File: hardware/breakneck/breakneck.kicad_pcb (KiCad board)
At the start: 2 copper layers, 53.3 x 64 mm, 112 parts, among them J1 CONN_WEST, J10 GS2, J12 CONN_JTAG_6P, J15 GS2, J16 CONN_JST, J2 CONN_DEDI, J3 CONN_OLED, J4 USB_C_Rcpt_Min, J5 CONN_SOUTH, J6 CONN_EAST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

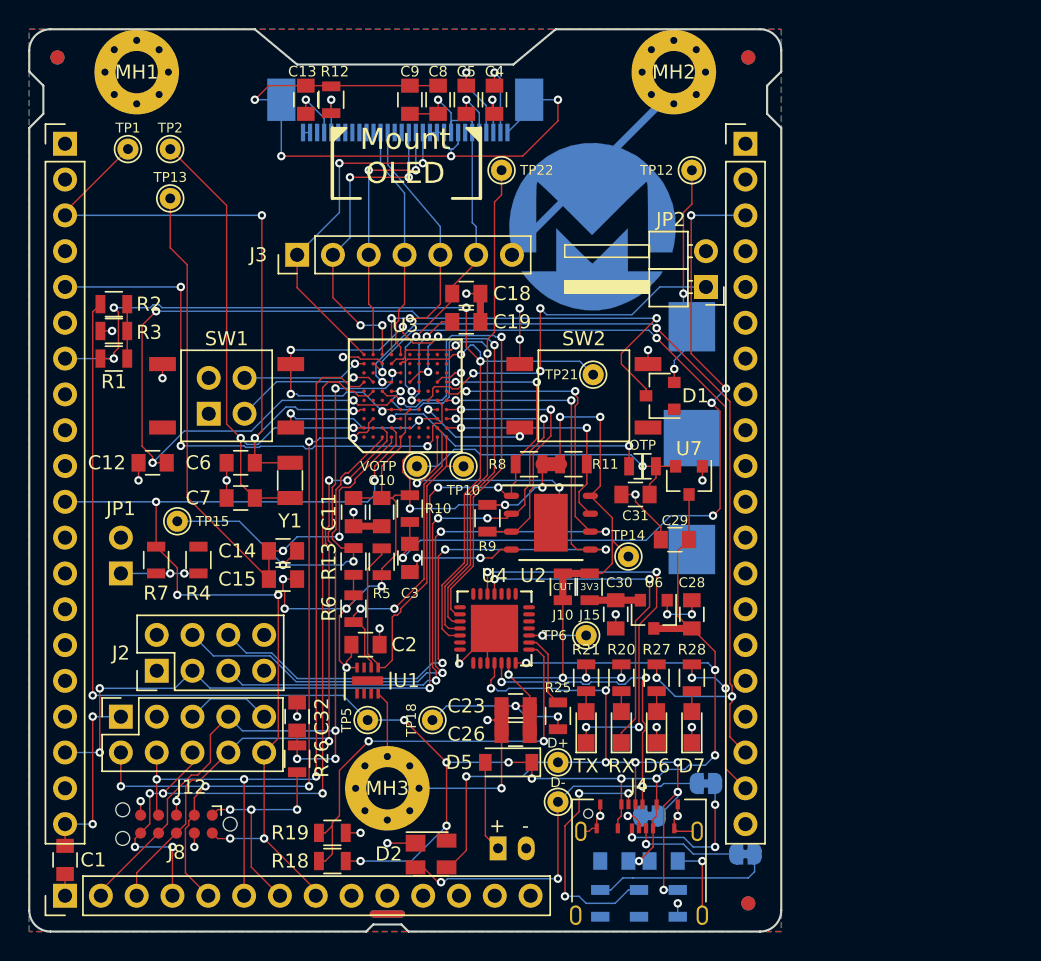
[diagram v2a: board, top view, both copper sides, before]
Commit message: Added slide switch (hack) and supporting circuitry to decouple lipo.
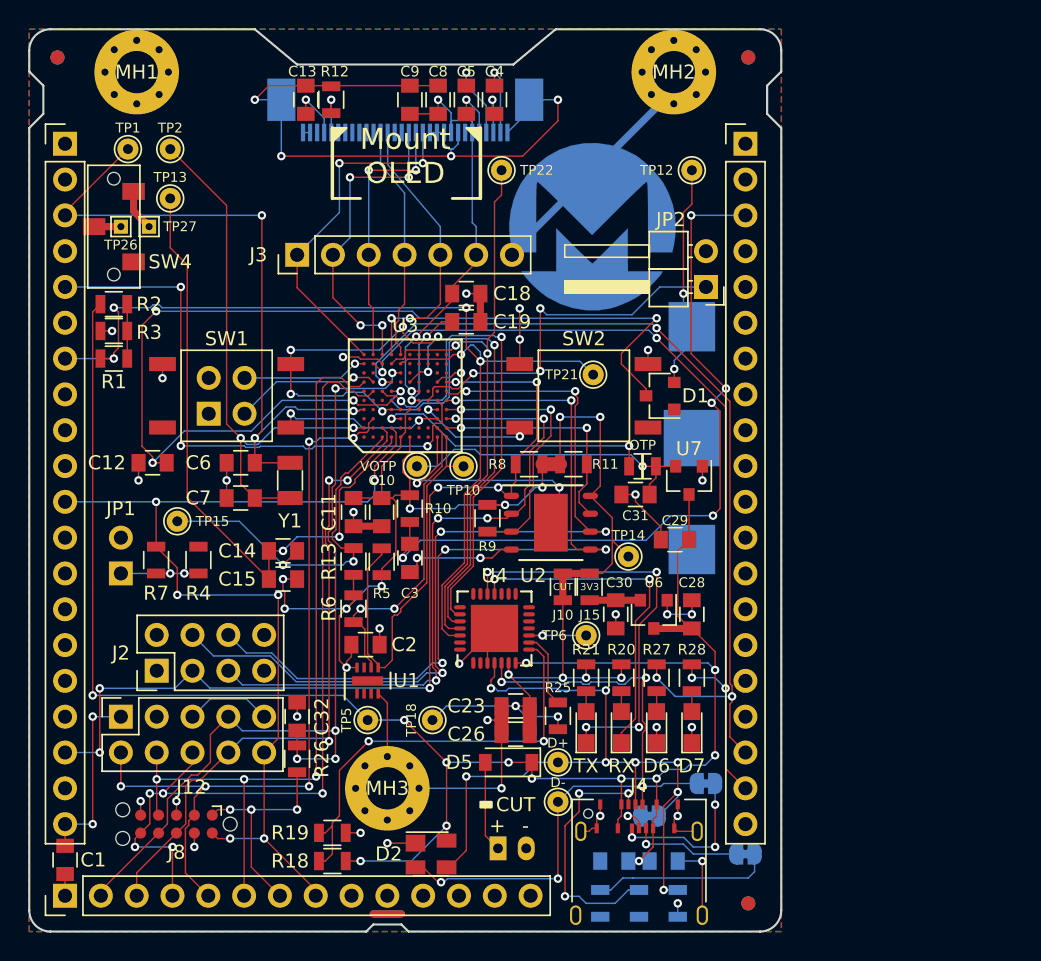
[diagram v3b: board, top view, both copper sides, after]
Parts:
- added SW4: SW_SPDT, Monero_Local:SW_SPDT_CLSB-12A, F.Cu at (106.0, 78.0)
- added TP26: TEST, Monero_Local:TestPoint_THTPad_1.0x1.0mm_Drill0.5mm, F.Cu at (106.5, 78.0)
- added TP27: TEST, Monero_Local:TestPoint_THTPad_1.0x1.0mm_Drill0.5mm, F.Cu at (108.5, 78.0)
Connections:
- J16 pad 1: Net-(D5-Pad2) -> Net-(J16-Pad1)
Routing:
- net Net-(J16-Pad1): track 0.00 -> 2.96 mm
- net Net-(D5-Pad2): track 6.47 -> 8.37 mm
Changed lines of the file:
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@@
   (general
     (thickness 1.6)
-    (drawings 146)
-    (tracks 1271)
+    (drawings 148)
+    (tracks 1274)
     (zones 0)
-    (modules 112)
-    (nets 161)
+    (modules 115)
+    (nets 163)
   )
   (page A4)
@@
   (net 159 "Net-(J4-PadB6)")
   (net 160 "Net-(JP5-Pad2)")
+  (net 161 "Net-(J16-Pad1)")
+  (net 162 "Net-(SW4-Pad1)")
   (net_class Default "This is the default net class."
     (clearance 0.1016)
@@
     (add_net "Net-(J1-Pad17)")
     (add_net "Net-(J1-Pad9)")
+    (add_net "Net-(J16-Pad1)")
     (add_net "Net-(J2-Pad7)")
     (add_net "Net-(J2-Pad8)")
@@
     (add_net "Net-(SW2-Pad2)")
     (add_net "Net-(SW3-Pad2)")
+    (add_net "Net-(SW4-Pad1)")
     (add_net "Net-(TP6-Pad1)")
     (add_net "Net-(U1-Pad1)")
@@
       (net 1 GND))
     (pad 1 thru_hole rect (at 0 0) (size 1.2 1.7) (drill 0.7) (layers *.Cu *.Mask)
-      (net 53 "Net-(D5-Pad2)"))
+      (net 161 "Net-(J16-Pad1)"))
     (model ${KIPRJMOD}/modules/packages3d/Connectors_JST.3dshapes/JST_PH_B2B-PH-K_02x2.00mm_Straight.wrl
       (at (xyz 0 0 0))
@@
       ))
   )
+  (module Monero_Local:SW_SPDT_CLSB-12A (layer F.Cu)
+    (at 106 78 90)
+    (descr https://www.nidec-copal-electronics.com/e/catalog/switch/cl-sb.pdf)
+    (tags "switch spdt")
+    (attr smd)
+    (fp_text reference SW4 (at -2.5 4 180) (layer F.SilkS)
+      (effects (font (size 1 1) (thickness 0.15)))
+    )
+    (fp_text value SW_SPDT (at 0 3.81 90) (layer F.Fab)
+      (effects (font (size 1 1) (thickness 0.15)))
+    )
+    (fp_line (start -4.25 -1.75) (end 4.25 -1.75) (layer F.Fab) (width 0.1))
+    (fp_line (start 4.25 -1.75) (end 4.25 1.75) (layer F.Fab) (width 0.1))
+    (fp_line (start 4.25 1.75) (end -4.25 1.75) (layer F.Fab) (width 0.1))
+    (fp_line (start -4.25 -1.75) (end -4.25 1.75) (layer F.Fab) (width 0.1))
+    (fp_text user %R (at 0 0 90) (layer F.Fab)
+      (effects (font (size 1 1) (thickness 0.15)))
+    )
+    (fp_line (start -4.35 -1.85) (end 4.35 -1.85) (layer F.SilkS) (width 0.12))
+    (fp_line (start 4.35 -1.85) (end 4.35 1.85) (layer F.SilkS) (width 0.12))
+    (fp_line (start -4.35 1.85) (end -4.35 -1.85) (layer F.SilkS) (width 0.12))
+    (fp_line (start -4.35 1.85) (end 4.35 1.85) (layer F.SilkS) (width 0.12))
+    (fp_line (start -4.75 -2.25) (end -4.75 2.25) (layer F.CrtYd) (width 0.05))
+    (fp_line (start -4.75 2.25) (end 4.75 2.25) (layer F.CrtYd) (width 0.05))
+    (fp_line (start 4.75 2.25) (end 4.75 -2.25) (layer F.CrtYd) (width 0.05))
+    (fp_line (start -4.75 -2.25) (end 4.75 -2.25) (layer F.CrtYd) (width 0.05))
+    (pad 1 smd rect (at -2.5 1.4 90) (size 1.2 1.6) (layers F.Cu F.Paste F.Mask)
+      (net 162 "Net-(SW4-Pad1)"))
+    (pad 2 smd rect (at 0 -1.4 90) (size 1.2 1.6) (layers F.Cu F.Paste F.Mask)
+      (net 53 "Net-(D5-Pad2)"))
+    (pad 3 smd rect (at 2.5 1.4 90) (size 1.2 1.6) (layers F.Cu F.Paste F.Mask)
+      (net 161 "Net-(J16-Pad1)"))
+    (pad "" np_thru_hole circle (at -3.4 0 90) (size 0.9 0.9) (drill 0.9) (layers *.Cu *.Mask))
+    (pad "" np_thru_hole circle (at 3.4 0 90) (size 0.9 0.9) (drill 0.9) (layers *.Cu *.Mask))
+    (model ${KIPRJMOD}/modules/packages3d/Buttons_Switches_SMD.3dshapes/SW_SPDT_CLSB-12A.wrl
+      (offset (xyz 0 0 3.5))
+      (scale (xyz 0.4 0.4 0.4))
+      (rotate (xyz -90 0 0))
+    )
+  )
+  (module Monero_Local:TestPoint_THTPad_1.0x1.0mm_Drill0.5mm (layer F.Cu)
+    (at 106.5 78)
+    (descr "THT rectangular pad as test Point, square 1.0mm side length, hole diameter 0.5mm")
+    (tags "test point THT pad rectangle square")
+    (attr virtual)
+    (fp_text reference TP26 (at 0 1.3) (layer F.SilkS)
+      (effects (font (size 0.7 0.7) (thickness 0.1)))
+    )
+    (fp_text value TEST (at 0 1.55) (layer F.Fab)
+      (effects (font (size 1 1) (thickness 0.15)))
+    )
+    (fp_line (start 1 1) (end -1 1) (layer F.CrtYd) (width 0.05))
+    (fp_line (start 1 1) (end 1 -1) (layer F.CrtYd) (width 0.05))
+    (fp_line (start -1 -1) (end -1 1) (layer F.CrtYd) (width 0.05))
+    (fp_line (start -1 -1) (end 1 -1) (layer F.CrtYd) (width 0.05))
+    (fp_line (start -0.7 0.7) (end -0.7 -0.7) (layer F.SilkS) (width 0.12))
+    (fp_line (start 0.7 0.7) (end -0.7 0.7) (layer F.SilkS) (width 0.12))
+    (fp_line (start 0.7 -0.7) (end 0.7 0.7) (layer F.SilkS) (width 0.12))
+    (fp_line (start -0.7 -0.7) (end 0.7 -0.7) (layer F.SilkS) (width 0.12))
+    (fp_text user %R (at 0 -1.45) (layer F.Fab)
+      (effects (font (size 1 1) (thickness 0.15)))
+    )
+    (pad 1 thru_hole rect (at 0 0) (size 1 1) (drill 0.5) (layers *.Cu *.Mask)
+      (net 53 "Net-(D5-Pad2)"))
+  )
+  (module Monero_Local:TestPoint_THTPad_1.0x1.0mm_Drill0.5mm (layer F.Cu)
+    (at 108.5 78)
+    (descr "THT rectangular pad as test Point, square 1.0mm side length, hole diameter 0.5mm")
+    (tags "test point THT pad rectangle square")
+    (attr virtual)
+    (fp_text reference TP27 (at 2.2 0) (layer F.SilkS)
+      (effects (font (size 0.7 0.7) (thickness 0.1)))
+    )
+    (fp_text value TEST (at 0 1.55) (layer F.Fab)
+      (effects (font (size 1 1) (thickness 0.15)))
+    )
+    (fp_text user %R (at 0 -1.45) (layer F.Fab)
+      (effects (font (size 1 1) (thickness 0.15)))
+    )
+    (fp_line (start -0.7 -0.7) (end 0.7 -0.7) (layer F.SilkS) (width 0.12))
+    (fp_line (start 0.7 -0.7) (end 0.7 0.7) (layer F.SilkS) (width 0.12))
+    (fp_line (start 0.7 0.7) (end -0.7 0.7) (layer F.SilkS) (width 0.12))
+    (fp_line (start -0.7 0.7) (end -0.7 -0.7) (layer F.SilkS) (width 0.12))
+    (fp_line (start -1 -1) (end 1 -1) (layer F.CrtYd) (width 0.05))
+    (fp_line (start -1 -1) (end -1 1) (layer F.CrtYd) (width 0.05))
+    (fp_line (start 1 1) (end 1 -1) (layer F.CrtYd) (width 0.05))
+    (fp_line (start 1 1) (end -1 1) (layer F.CrtYd) (width 0.05))
+    (pad 1 thru_hole rect (at 0 0) (size 1 1) (drill 0.5) (layers *.Cu *.Mask)
+      (net 161 "Net-(J16-Pad1)"))
+  )
+  (gr_poly (pts (xy 132 119.2) (xy 132.8 119.2) (xy 132.8 118.8) (xy 132 118.8)) (layer F.SilkS) (width 0.15))
+  (gr_text CUT (at 134.5 119) (layer F.SilkS)
+    (effects (font (size 1 1) (thickness 0.2)))
+  )
   (dimension 64 (width 0.3) (layer Dwgs.User)
     (gr_text "64,000 mm" (at 94.15 96 270) (layer Dwgs.User)
@@
   (segment (start 143.702401 113.697599) (end 143.5 113.9) (width 0.1016) (layer F.Cu) (net 31))
   (segment (start 142.25 110.46) (end 142.71 110) (width 0.1016) (layer B.Cu) (net 31))
-  (segment (start 142.75 121.325) (end 142.75 120.68) (width 0.1016) (layer F.Cu) (net 158) (status 30))
   (segment (start 143.5 117.7) (end 143.5 118.98) (width 0.1016) (layer F.Cu) (net 31) (status 20))
   (via (at 143.5 117.7) (size 0.6) (drill 0.3) (layers F.Cu B.Cu) (net 31))
@@
   (segment (start 143.5 117.7) (end 144.8 117.7) (width 0.1016) (layer B.Cu) (net 31))
   (segment (start 144.8 117.7) (end 145 117.5) (width 0.1016) (layer B.Cu) (net 31))
-  (via (at 142.75 121.325) (size 0.6) (drill 0.3) (layers F.Cu B.Cu) (net 158))
   (via (at 132.75 110.75) (size 0.6) (drill 0.3) (layers F.Cu B.Cu) (net 32))
   (segment (start 133 108.95) (end 133 109.910814) (width 0.1016) (layer F.Cu) (net 32) (status 10))
@@
   (segment (start 132.35 121.2) (end 133.25 122.1) (width 0.1016) (layer F.Cu) (net 53) (status 20))
   (segment (start 132.35 116) (end 132.35 121.2) (width 0.1016) (layer F.Cu) (net 53) (status 10))
+  (segment (start 104.6 78) (end 106.5 78) (width 0.508) (layer F.Cu) (net 53))
   (via (at 128.25 93.575) (size 0.6) (drill 0.3) (layers F.Cu B.Cu) (net 57))
   (segment (start 129.275 91.853351) (end 129.275 90.655) (width 0.1016) (layer F.Cu) (net 57))
@@
   (segment (start 144.5 112.4) (end 144.5 110.95) (width 0.1016) (layer F.Cu) (net 156) (status 30))
   (segment (start 147 112.4) (end 147 110.95) (width 0.1016) (layer F.Cu) (net 157) (status 30))
+  (segment (start 142.75 121.325) (end 142.75 120.68) (width 0.1016) (layer F.Cu) (net 158) (status 30))
+  (via (at 142.75 121.325) (size 0.6) (drill 0.3) (layers F.Cu B.Cu) (net 158))
   (via (at 148.65 119) (size 0.6) (drill 0.3) (layers F.Cu B.Cu) (net 158))
   (segment (start 148.65 117.5) (end 148.65 119) (width 0.1016) (layer B.Cu) (net 158))
@@
   (segment (start 151.45 122.5) (end 151.45 123.75) (width 0.1016) (layer B.Cu) (net 160))
   (segment (start 142.825678 124.2) (end 151 124.2) (width 0.1016) (layer B.Cu) (net 160))
+  (segment (start 107.4 76.9) (end 108.5 78) (width 0.508) (layer F.Cu) (net 161))
+  (segment (start 107.4 75.5) (end 107.4 76.9) (width 0.508) (layer F.Cu) (net 161))
   (zone (net 3) (net_name +3V3) (layer F.Cu) (hatch edge 0.508)
     (connect_pads (clearance 0.508))

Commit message: Bumped revision identifiers and legal text pending new year of the pig.
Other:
- board text added: "Seventh generation prototype RFC-HWALLET-1 ET1 Extra Tabulo, by the Monero Hardware Team CERN OSH License, © 2019 The Monero Project"
- board text removed: "Fifth generation prototype RFC-HWALLET-1 ET1 Extra Tabulo, by the Monero Hardware Team CERN OSH License, © 2018 The Monero Project"
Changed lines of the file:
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@@
     (title "Breakneck Hardware Wallet")
     (date 2018-01-10)
-    (rev 0.9.1)
+    (rev 0.9.2)
     (company "The Monero Project, Hardware Team")
-    (comment 1 "Copyright © 2018, The Monero Project")
+    (comment 1 "Copyright © 2019, The Monero Project")
     (comment 2 "Fulfilling the developer edition role")
     (comment 3 "Pending quality assurance testing")
@@
   (gr_line (start 148.5 60) (end 148.5 132) (angle 90) (layer F.CrtYd) (width 0.2))
   (gr_line (start 105 60) (end 105 132) (angle 90) (layer F.CrtYd) (width 0.2))
-  (gr_text "Fifth generation prototype RFC-HWALLET-1\nET1 Extra Tabulo, by the Monero Hardware Team\nCERN OSH License, © 2018 The Monero Project" (at 145 87) (layer B.SilkS)
+  (gr_text "Seventh generation prototype RFC-HWALLET-1\nET1 Extra Tabulo, by the Monero Hardware Team\nCERN OSH License, © 2019 The Monero Project" (at 145 87) (layer B.SilkS)
     (effects (font (size 1 1) (thickness 0.2)) (justify left mirror))
   )

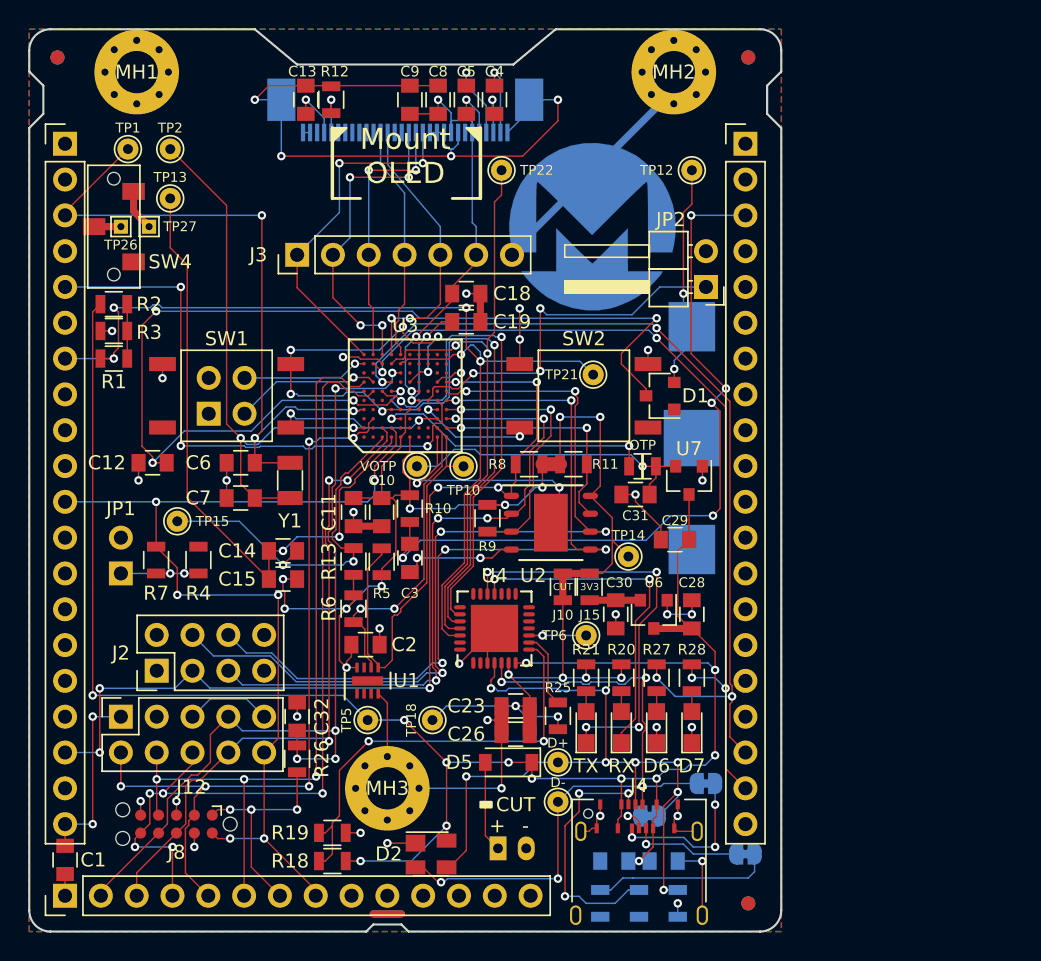
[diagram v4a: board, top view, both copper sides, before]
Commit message: Merged a932921 from 'revstm' adding a intrusion detector switch.
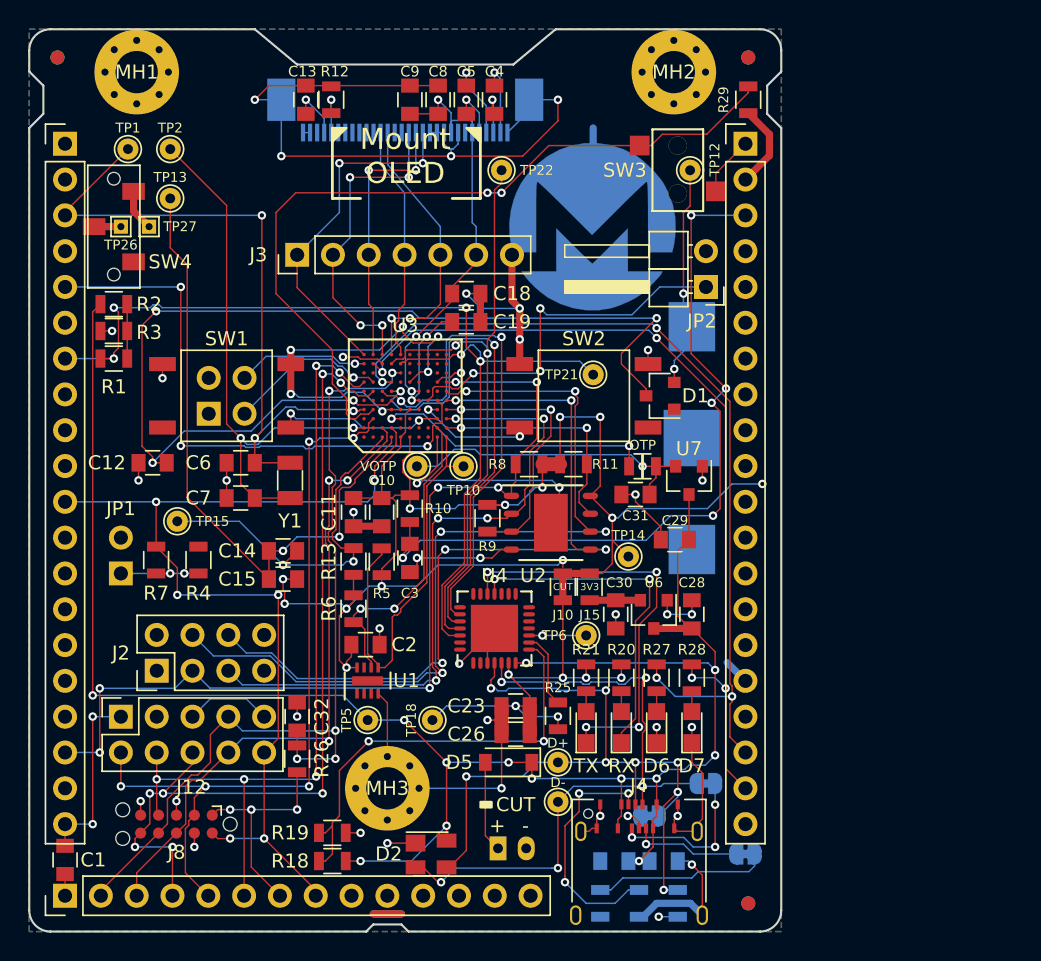
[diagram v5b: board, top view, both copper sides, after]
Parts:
- added R29: 10K, Monero_Local:R_0805, F.Cu at (151.0, 69.0)
- added SW3: SW_SPST, Monero_Local:SW_SPST_ESE11MV1, F.Cu at (146.0, 74.0)
- moved TP12 0.12 mm to (146.9, 74.0)
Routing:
- net Net-(R29-Pad2): track 0.00 -> 56.1 mm, vias 0 -> 2
- net +3V3: track 150.6 -> 182.7 mm, vias 21 -> 24
- net GND: track 218.5 -> 226.8 mm
- net (no net): track 0.00 -> 2.00 mm
- net /JTAG_TCK: track 56.0 -> 57.4 mm, vias 3 -> 5
- net /SAO_SCL: track 10.3 -> 11.4 mm
- net /JTAG_TDO: track 59.4 -> 60.5 mm, vias 5 -> 7
- net Net-(J4-PadA5): track 17.8 -> 17.3 mm
- net /JTAG_TRST: track 61.6 -> 62.1 mm
